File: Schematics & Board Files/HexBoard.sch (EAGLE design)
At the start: 26 parts

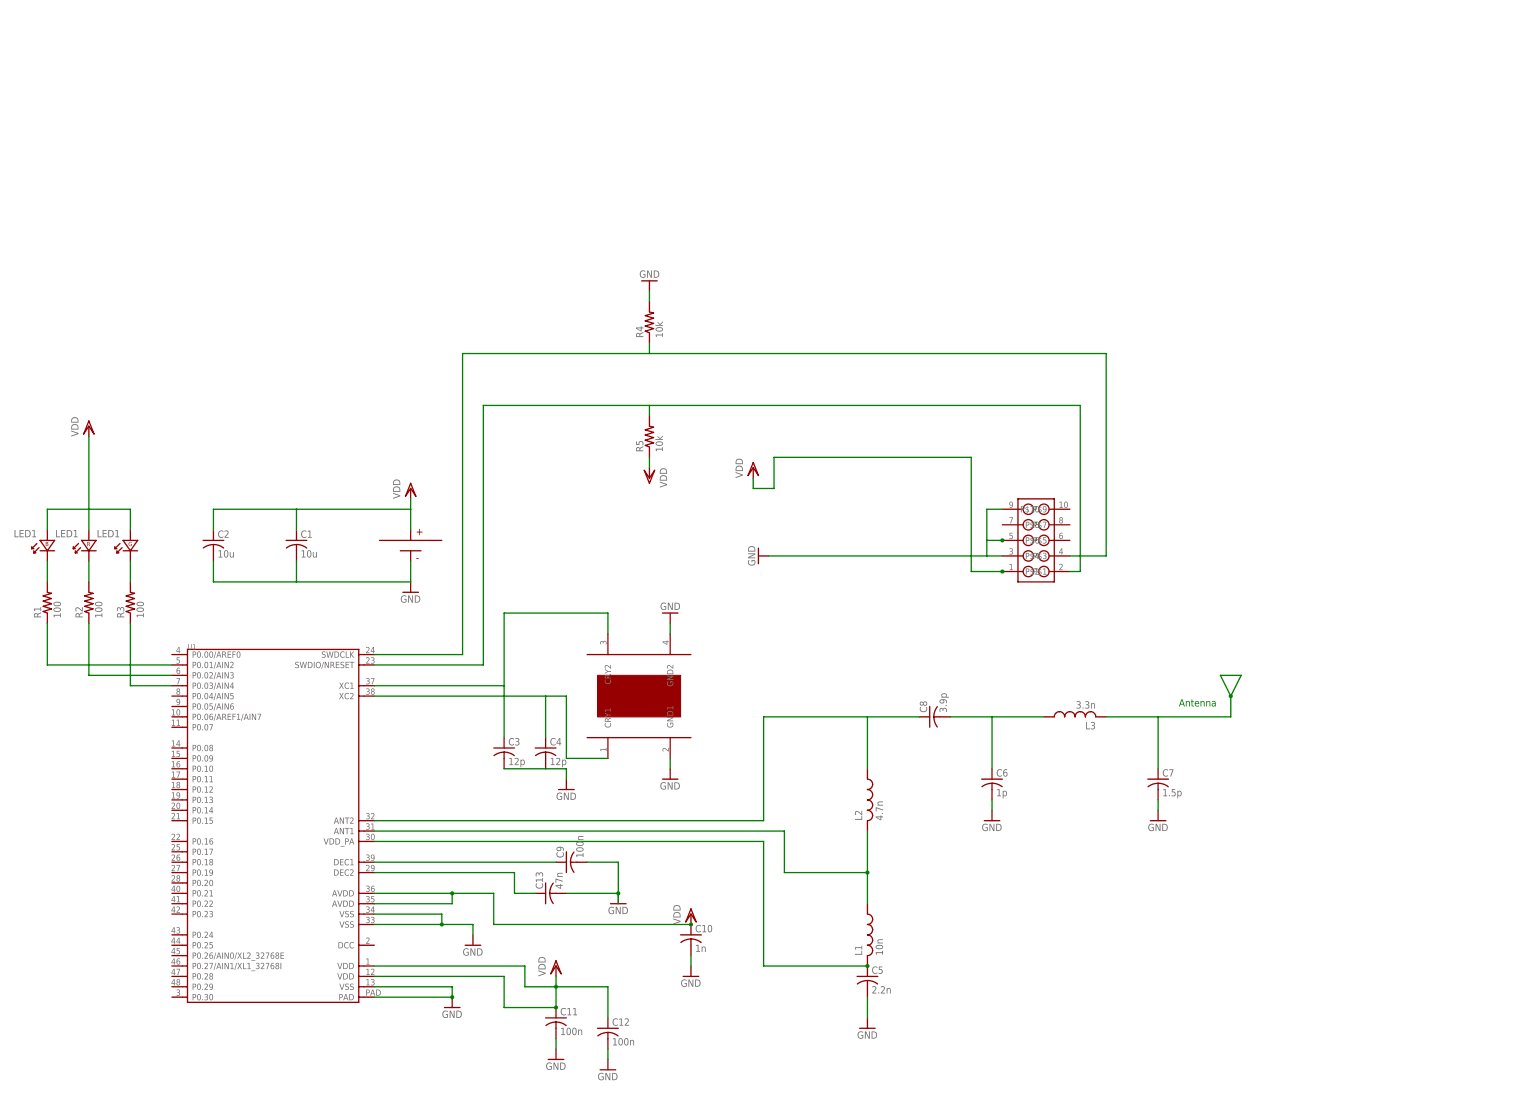
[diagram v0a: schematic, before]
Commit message: Schematic clean up
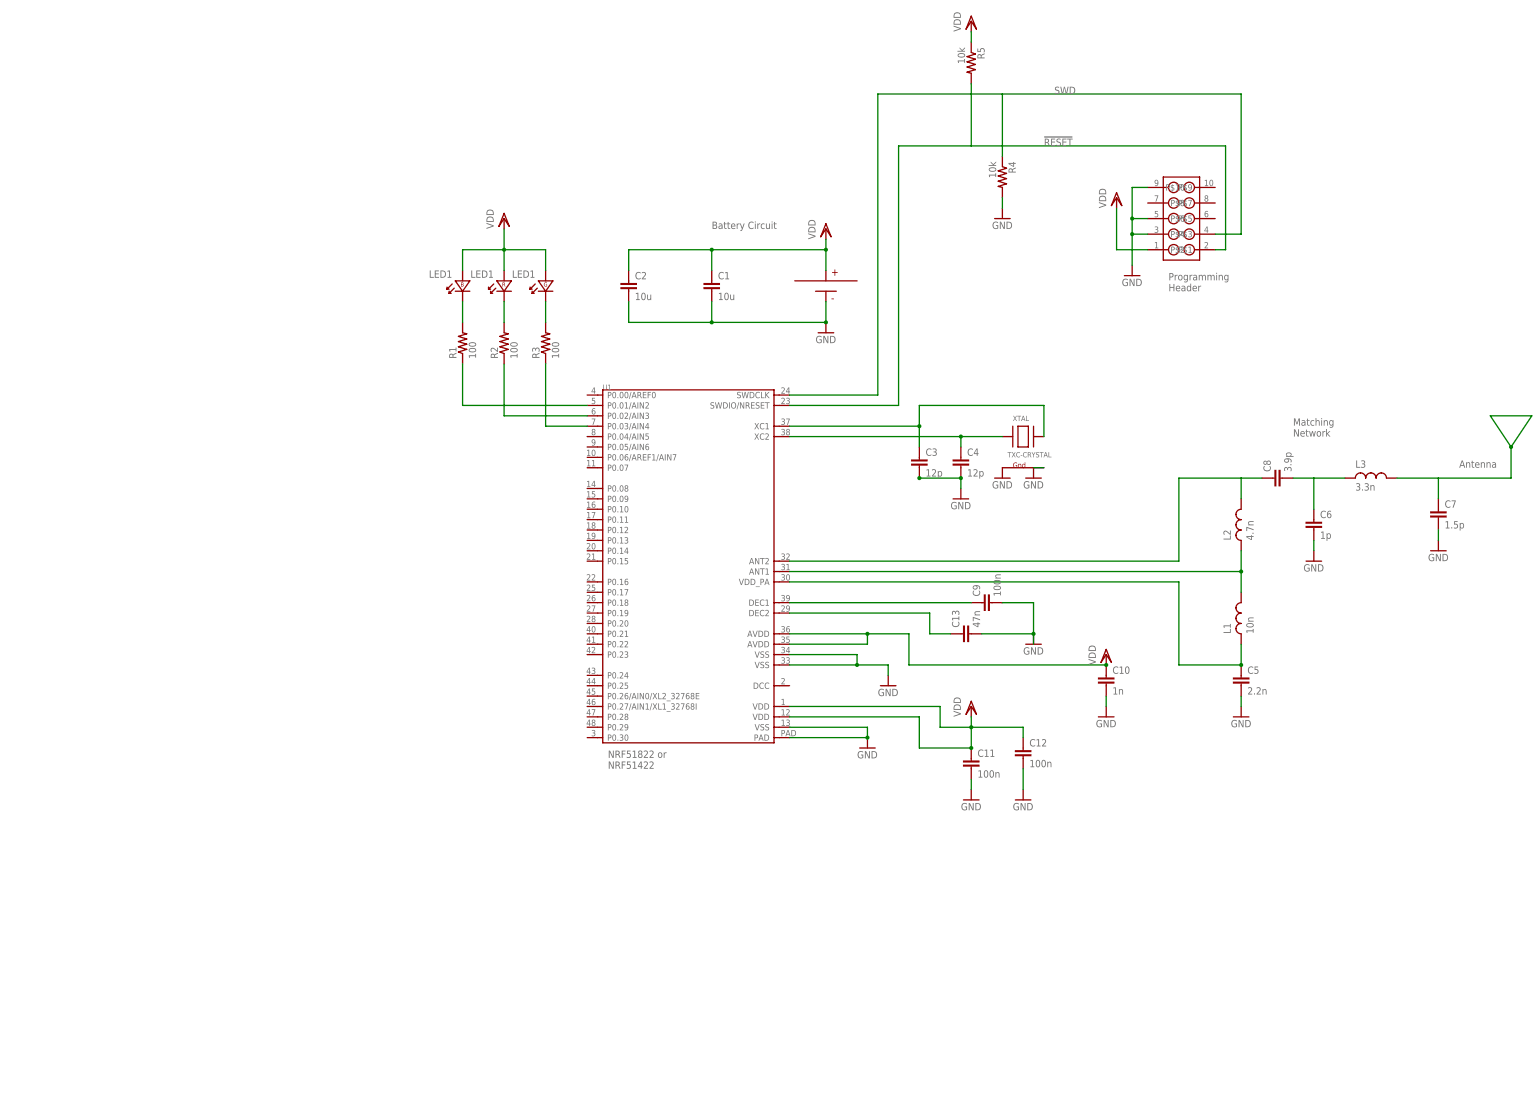
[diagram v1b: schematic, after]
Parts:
- C1, C2: device adafruit:C-USC0805K -> rcl:C-EUC0805
- C10, C11, C12, C3, C4, C5, C6, C7, C8, C9: device adafruit:C-USC0402 -> rcl:C-EUC0402
- C13: device adafruit:C-USC0603K -> rcl:C-EUC0402
- L1, L2, L3: device CHIP_INDUCTOR:402_CHIP_INDUCTOR -> rcl_custom:L-US0402-B-NOSILK
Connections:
- net N$10 renamed !RESET
- net N$7 renamed SWD
- removed net N$8: C3.1, U1.XC1, XTAL.CRY2
- new net XTAL: C3.1, U1.XC1, XTAL.X2
- net GND: now also XTAL.G1, XTAL.G2; no longer XTAL.GND1, XTAL.GND2
- net N$11: now also L1.2, L2.1; no longer L1.1, L2.2
- net N$15: now also L2.2; no longer L2.1
- net N$17: now also L1.1; no longer L1.2
- net N$9: now also XTAL.X1; no longer XTAL.CRY1
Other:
- note added: "Battery Circuit"
- note added: "Matching Network"
- note added: "NRF51822 or NRF51422"
- note added: "Programming Header"
- moved on the sheet: C1, C10, C11, C12, C13, C2, C3, C4, C5, C6, C7, C8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
